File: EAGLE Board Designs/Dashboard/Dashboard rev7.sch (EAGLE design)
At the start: 118 parts, among them J1 CONNECTOR-4_μF_S_RA_, J10 CONNECTOR-10__, J11 CONNECTOR-8_μF_S_RA_, J2 CONNECTOR-8_μF_S_RA_, J3 CONNECTOR-4_μF_S_RA_, J4 CONNECTOR-6_μF_S_RA_, J5 CONNECTOR-10__, J7 CONNECTOR-4_538-505110-0492_, J8 USB4110, J9 CONNECTOR-4_538-505110-0492_, U1 NEOPIXEL_IN-PI55QATPRPGPBPW-40, U10 NEOPIXEL_IN-PI55QATPRPGPBPW-40, U12 NEOPIXEL_IN-PI55QATPRPGPBPW-40, U13 NEOPIXEL_IN-PI55QATPRPGPBPW-40, U14 NEOPIXEL_IN-PI55QATPRPGPBPW-40, U15 NEOPIXEL_IN-PI55QATPRPGPBPW-40, U16 STM32-LQFP64, U17 VOLTAGE_REGULATOR_SOT-223_3.3V, U2 NEOPIXEL_IN-PI55QATPRPGPBPW-40, U27 TCAN1051HQV-Q1, U3 MCP23S08, U4 NEOPIXEL_IN-PI55QATPRPGPBPW-40, U5 RE46C100, U6 NEOPIXEL_IN-PI55QATPRPGPBPW-40, U7 NEOPIXEL_IN-PI55QATPRPGPBPW-40, U8 NEOPIXEL_IN-PI55QATPRPGPBPW-40, U9 NEOPIXEL_IN-PI55QATPRPGPBPW-40, X1 24_MHZ_XTAL_OSCILLATOR

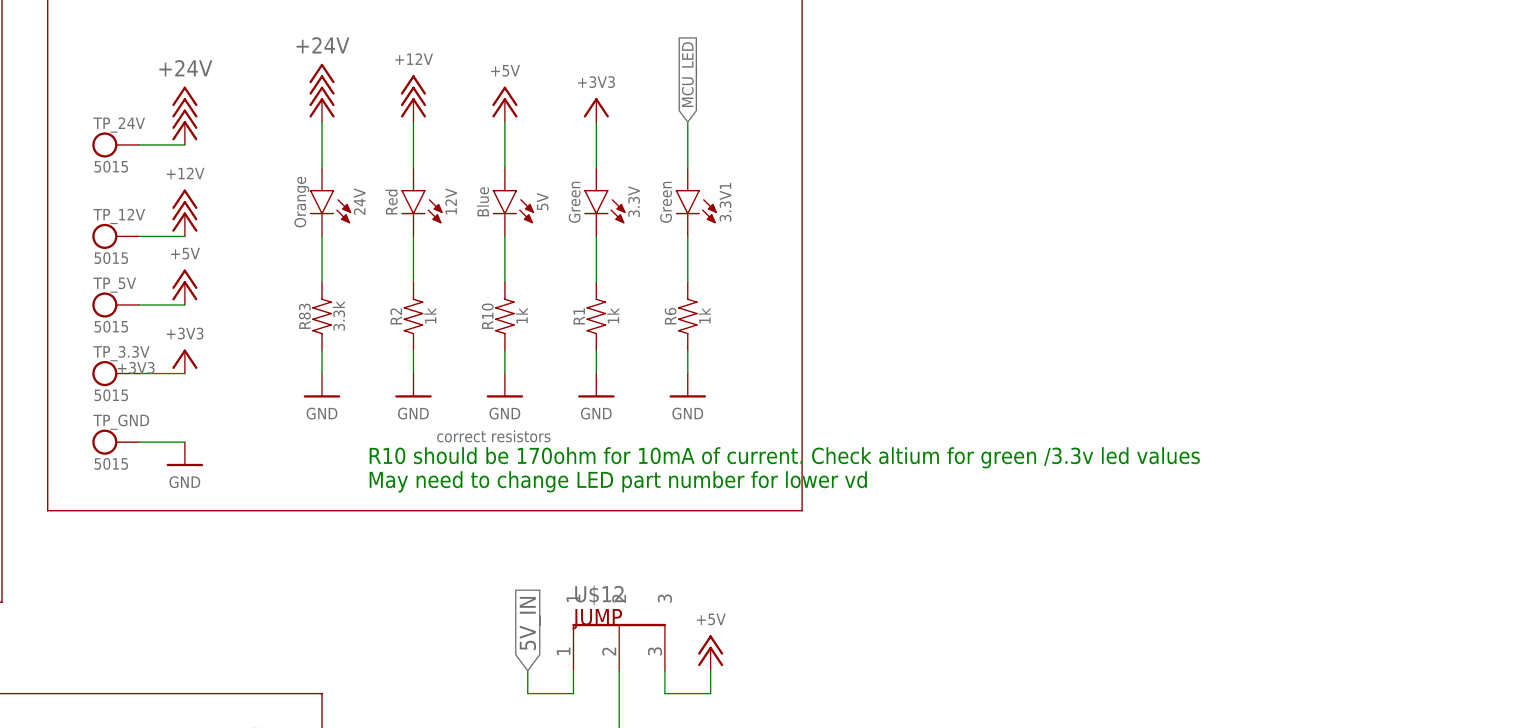
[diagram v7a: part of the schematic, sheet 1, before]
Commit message: Changed LEDs and Resistor values
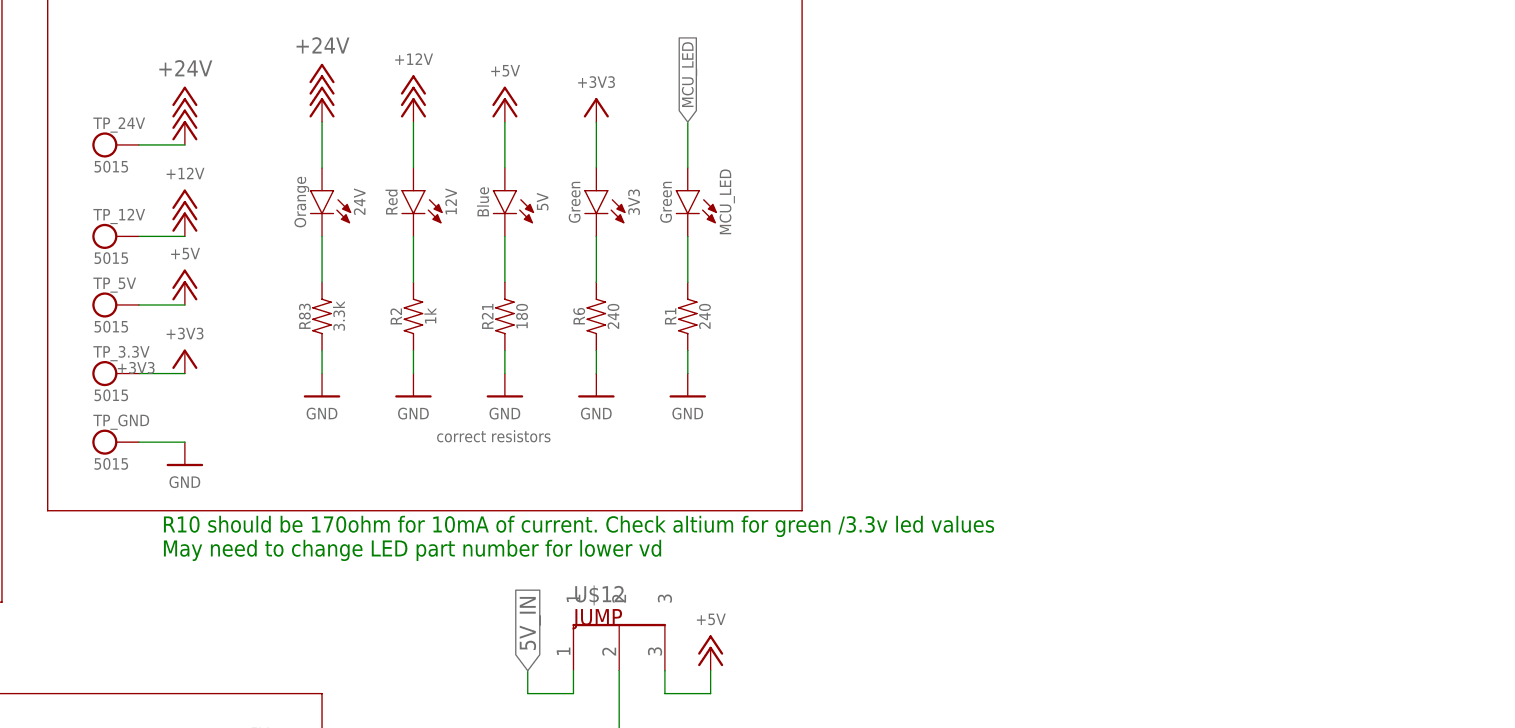
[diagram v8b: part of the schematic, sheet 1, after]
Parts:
- removed 3.3V, 3.3V1: LED_0603_GREEN, HyTechDevices - Copy:LED_0603_GREEN
- removed R10: RESISTOR_0603_1K, HyTechDevices:RESISTOR_0603_1K
- added 3V3, MCU_LED: LED_0603_GREEN_2V2, HyTechDevices:LED_0603_GREEN_2V2
- added R21: RESISTOR_0603_180, HyTechDevices:RESISTOR_0603_180
- R1, R6: value RESISTOR_0603_1K -> RESISTOR_0603_240; device HyTechDevices:RESISTOR_0603_1K -> HyTechDevices:RESISTOR_0603_240
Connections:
- net +3V3: now also 3V3.A; no longer 3.3V.A
- net GND: now also R21.1; no longer R10.1
- net MCU_LED: now also MCU_LED.A; no longer 3.3V1.A
- net N$11: now also MCU_LED.C, R1.2; no longer 3.3V1.C, R6.2
- net N$31: now also 3V3.C, R6.2; no longer 3.3V.C, R1.2
- net N$32: now also R21.2; no longer R10.2
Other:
- moved on the sheet: R1, R6
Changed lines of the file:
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@@
 <part name="P52" library="HyTechSupplies" deviceset="+12V" device=""/>
 <part name="P55" library="HyTechSupplies" deviceset="+5V" device=""/>
-<part name="R10" library="HyTechDevices" deviceset="RESISTOR_?_*" device="0603" technology="1K"/>
 <part name="5V" library="HyTechDevices - Copy" deviceset="LED_?_*" device="0603" technology="BLUE"/>
 <part name="12V" library="HyTechDevices - Copy" deviceset="LED_?_*" device="0603" technology="RED"/>
@@
 <part name="P75" library="HyTechSupplies" deviceset="GND" device=""/>
 <part name="P76" library="HyTechSupplies" deviceset="+3V3" device=""/>
-<part name="3.3V" library="HyTechDevices - Copy" deviceset="LED_?_*" device="0603" technology="GREEN"/>
-<part name="R1" library="HyTechDevices" deviceset="RESISTOR_?_*" device="0603" technology="1K"/>
 <part name="R2" library="HyTechDevices" deviceset="RESISTOR_?_*" device="0603" technology="1K"/>
 <part name="P110" library="HyTechSupplies" deviceset="GND" device=""/>
@@
 <part name="R16" library="HyTechDevices" deviceset="RESISTOR_?_*" device="0603" technology="10K"/>
 <part name="P63" library="HyTechSupplies" deviceset="GND" device=""/>
-<part name="3.3V1" library="HyTechDevices - Copy" deviceset="LED_?_*" device="0603" technology="GREEN"/>
-<part name="R6" library="HyTechDevices" deviceset="RESISTOR_?_*" device="0603" technology="1K"/>
 <part name="X1" library="HyTechTemp" deviceset="24_MHZ_XTAL_OSCILLATOR" device=""/>
 <part name="P31" library="HyTechSupplies" deviceset="GND" device=""/>
@@
 <part name="P43" library="HyTechSupplies" deviceset="+5V" device=""/>
 <part name="P88" library="HyTechSupplies" deviceset="+5V" device=""/>
+<part name="3V3" library="HyTechDevices" deviceset="LED_?_*" device="0603" technology="GREEN_2V2"/>
+<part name="MCU_LED" library="HyTechDevices" deviceset="LED_?_*" device="0603" technology="GREEN_2V2"/>
+<part name="R21" library="HyTechDevices" deviceset="RESISTOR_?_*" device="0603" technology="180"/>
+<part name="R1" library="HyTechDevices" deviceset="RESISTOR_?_*" device="0603" technology="240"/>
+<part name="R6" library="HyTechDevices" deviceset="RESISTOR_?_*" device="0603" technology="240"/>
 </parts>
 <sheets>
@@
 <text x="101.6" y="114.3" size="1.778" layer="97">Backlight 2</text>
 <text x="15.24" y="40.64" size="1.778" layer="97">Display</text>
-<text x="203.2" y="142.24" size="1.778" layer="91">R10 should be 170ohm for 10mA of current. Check altium for green /3.3v led values
+<text x="180.34" y="134.62" size="1.778" layer="91">R10 should be 170ohm for 10mA of current. Check altium for green /3.3v led values
 May need to change LED part number for lower vd</text>
 <text x="177.8" y="38.1" size="2.54" layer="97">Walker Burns</text>
@@
 <attribute name="VALUE" x="218.44" y="187.96" size="1.27" layer="96" align="bottom-center"/>
 </instance>
-<instance part="R10" gate="G$1" x="218.44" y="162.56" smashed="yes" rot="R90">
-<attribute name="NAME" x="217.17" y="161.29" size="1.27" layer="95" rot="R90" align="bottom-center"/>
-<attribute name="RESISTANCE" x="219.71" y="161.29" size="1.27" layer="96" rot="R90" align="top-center"/>
-</instance>
 <instance part="5V" gate="LED" x="218.44" y="172.72" smashed="yes" rot="R270">
 <attribute name="COLOR" x="216.662" y="173.99" size="1.27" layer="95" rot="R270" align="top-center"/>
@@
 <instance part="P76" gate="G$1" x="228.6" y="185.42" smashed="yes">
 <attribute name="VALUE" x="228.6" y="186.69" size="1.27" layer="96" align="bottom-center"/>
-</instance>
-<instance part="3.3V" gate="LED" x="228.6" y="172.72" smashed="yes" rot="R270">
-<attribute name="COLOR" x="226.822" y="173.99" size="1.27" layer="95" rot="R270" align="top-center"/>
-<attribute name="NAME" x="232.156" y="173.99" size="1.27" layer="96" rot="R270" align="bottom-center"/>
-</instance>
-<instance part="R1" gate="G$1" x="228.6" y="162.56" smashed="yes" rot="R90">
-<attribute name="NAME" x="227.33" y="161.29" size="1.27" layer="95" rot="R90" align="bottom-center"/>
-<attribute name="RESISTANCE" x="229.87" y="161.29" size="1.27" layer="96" rot="R90" align="top-center"/>
 </instance>
 <instance part="R2" gate="G$1" x="208.28" y="162.56" smashed="yes" rot="R90">
@@
 <attribute name="VALUE" x="238.76" y="151.13" size="1.27" layer="96" align="top-center"/>
 </instance>
-<instance part="3.3V1" gate="LED" x="238.76" y="172.72" smashed="yes" rot="R270">
-<attribute name="COLOR" x="236.982" y="173.99" size="1.27" layer="95" rot="R270" align="top-center"/>
-<attribute name="NAME" x="242.316" y="173.99" size="1.27" layer="96" rot="R270" align="bottom-center"/>
-</instance>
-<instance part="R6" gate="G$1" x="238.76" y="162.56" smashed="yes" rot="R90">
-<attribute name="NAME" x="237.49" y="161.29" size="1.27" layer="95" rot="R90" align="bottom-center"/>
-<attribute name="RESISTANCE" x="240.03" y="161.29" size="1.27" layer="96" rot="R90" align="top-center"/>
-</instance>
 <instance part="U17" gate="G$1" x="132.08" y="152.4" smashed="yes">
 <attribute name="NAME" x="132.08" y="153.162" size="1.27" layer="95"/>
@@
 <instance part="P88" gate="1" x="241.3" y="124.46" smashed="yes">
 <attribute name="VALUE" x="241.3" y="127" size="1.27" layer="96" align="bottom-center"/>
+</instance>
+<instance part="3V3" gate="LED" x="228.6" y="172.72" smashed="yes" rot="R270">
+<attribute name="COLOR" x="226.822" y="173.99" size="1.27" layer="95" rot="R270" align="top-center"/>
+<attribute name="NAME" x="232.156" y="173.99" size="1.27" layer="96" rot="R270" align="bottom-center"/>
+</instance>
+<instance part="MCU_LED" gate="LED" x="238.76" y="172.72" smashed="yes" rot="R270">
+<attribute name="COLOR" x="236.982" y="173.99" size="1.27" layer="95" rot="R270" align="top-center"/>
+<attribute name="NAME" x="242.316" y="173.99" size="1.27" layer="96" rot="R270" align="bottom-center"/>
+</instance>
+<instance part="R21" gate="G$1" x="218.44" y="162.56" smashed="yes" rot="R90">
+<attribute name="NAME" x="217.17" y="161.29" size="1.27" layer="95" rot="R90" align="bottom-center"/>
+<attribute name="RESISTANCE" x="219.71" y="161.29" size="1.27" layer="96" rot="R90" align="top-center"/>
+</instance>
+<instance part="R1" gate="G$1" x="238.76" y="162.56" smashed="yes" rot="R90">
+<attribute name="NAME" x="237.49" y="161.29" size="1.27" layer="95" rot="R90" align="bottom-center"/>
+<attribute name="RESISTANCE" x="240.03" y="161.29" size="1.27" layer="96" rot="R90" align="top-center"/>
+</instance>
+<instance part="R6" gate="G$1" x="228.6" y="162.56" smashed="yes" rot="R90">
+<attribute name="NAME" x="227.33" y="161.29" size="1.27" layer="95" rot="R90" align="bottom-center"/>
+<attribute name="RESISTANCE" x="229.87" y="161.29" size="1.27" layer="96" rot="R90" align="top-center"/>
 </instance>
 </instances>
@@
 </segment>
 <segment>
-<pinref part="R10" gate="G$1" pin="1"/>
 <pinref part="P57" gate="1" pin="GND"/>
 <wire x1="218.44" y1="157.48" x2="218.44" y2="154.94" width="0.1524" layer="91"/>
+<pinref part="R21" gate="G$1" pin="1"/>
 </segment>
 <segment>
 <pinref part="P75" gate="1" pin="GND"/>
 <wire x1="228.6" y1="157.48" x2="228.6" y2="154.94" width="0.1524" layer="91"/>
-<pinref part="R1" gate="G$1" pin="1"/>
+<pinref part="R6" gate="G$1" pin="1"/>
 </segment>
 <segment>
@@
 <pinref part="P63" gate="1" pin="GND"/>
 <wire x1="238.76" y1="157.48" x2="238.76" y2="154.94" width="0.1524" layer="91"/>
-<pinref part="R6" gate="G$1" pin="1"/>
+<pinref part="R1" gate="G$1" pin="1"/>
 </segment>
 <segment>
@@
 <net name="+3V3" class="0">
 <segment>
-<pinref part="3.3V" gate="LED" pin="A"/>
 <pinref part="P76" gate="G$1" pin="+3V3"/>
 <wire x1="228.6" y1="177.8" x2="228.6" y2="182.88" width="0.1524" layer="91"/>
+<pinref part="3V3" gate="LED" pin="A"/>
 </segment>
 <segment>
@@
 <net name="N$31" class="0">
 <segment>
-<pinref part="3.3V" gate="LED" pin="C"/>
 <wire x1="228.6" y1="165.1" x2="228.6" y2="170.18" width="0.1524" layer="91"/>
-<pinref part="R1" gate="G$1" pin="2"/>
+<pinref part="3V3" gate="LED" pin="C"/>
+<pinref part="R6" gate="G$1" pin="2"/>
 </segment>
 </net>
 <net name="N$32" class="0">
 <segment>
-<pinref part="R10" gate="G$1" pin="2"/>
 <pinref part="5V" gate="LED" pin="C"/>
 <wire x1="218.44" y1="170.18" x2="218.44" y2="165.1" width="0.1524" layer="91"/>
+<pinref part="R21" gate="G$1" pin="2"/>
 </segment>
 </net>
@@
 <net name="N$11" class="0">
 <segment>
-<pinref part="3.3V1" gate="LED" pin="C"/>
 <wire x1="238.76" y1="165.1" x2="238.76" y2="170.18" width="0.1524" layer="91"/>
-<pinref part="R6" gate="G$1" pin="2"/>
+<pinref part="MCU_LED" gate="LED" pin="C"/>
+<pinref part="R1" gate="G$1" pin="2"/>
 </segment>
 </net>
 <net name="MCU_LED" class="0">
 <segment>
-<pinref part="3.3V1" gate="LED" pin="A"/>
 <wire x1="238.76" y1="177.8" x2="238.76" y2="182.88" width="0.1524" layer="91"/>
 <label x="238.76" y="182.88" size="1.27" layer="95" font="vector" rot="R90" xref="yes"/>
-</segment>
-</net>
+<pinref part="MCU_LED" gate="LED" pin="A"/>
+</segment>
+</net>
